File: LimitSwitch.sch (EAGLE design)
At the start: 4 parts

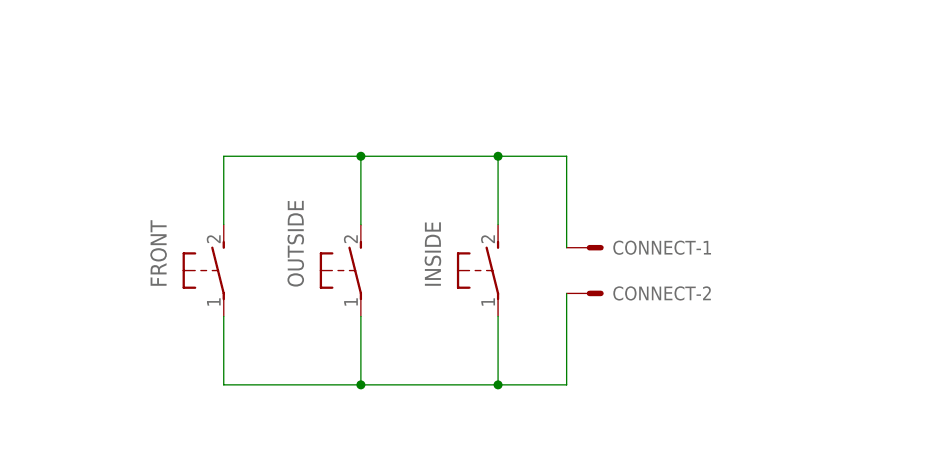
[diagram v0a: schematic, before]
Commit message: much smaller switch
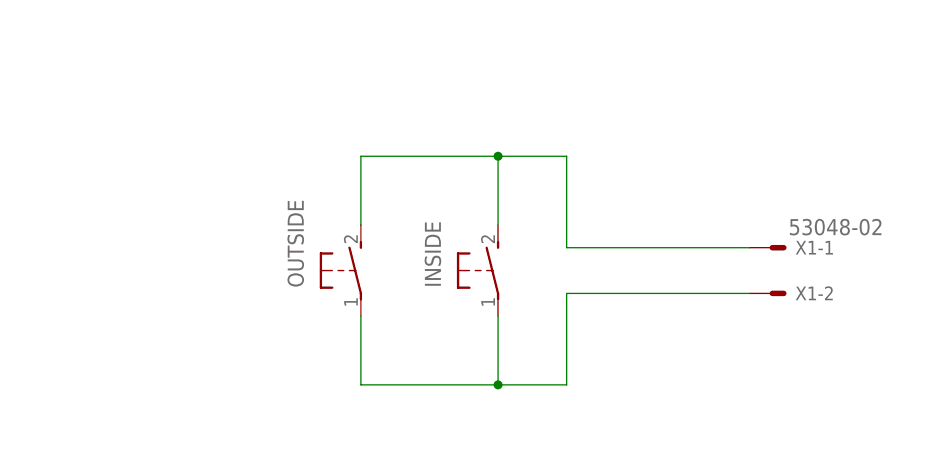
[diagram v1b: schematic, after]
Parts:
- removed CONNECT: (no value), con-molex-2:555X-2H
- removed FRONT: (no value), switch-omron:31-XX
- added X1: 53048-02, con-molex:53048-02
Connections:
- net +: now also X1-1.S; no longer CONNECT-1.S, FRONT.S
- net GND: now also X1-2.S; no longer CONNECT-2.S, FRONT.P
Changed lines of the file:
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@@
 <setting verticaltext="up"/>
 </settings>
-<grid distance="0.1" unitdist="inch" unit="inch" style="lines" multiple="1" display="yes" altdistance="0.01" altunitdist="inch" altunit="inch"/>
+<grid distance="0.1" unitdist="inch" unit="inch" style="lines" multiple="1" display="no" altdistance="0.01" altunitdist="inch" altunit="inch"/>
 <layers>
 <layer number="1" name="Top" color="4" fill="1" visible="no" active="no"/>
@@
 <parts>
 <part name="INSIDE" library="switch-omron" deviceset="31-XX" device=""/>
-<part name="CONNECT" library="con-molex-2" deviceset="555X-2" device="H"/>
 <part name="OUTSIDE" library="switch-omron" deviceset="31-XX" device=""/>
-<part name="FRONT" library="switch-omron" deviceset="31-XX" device=""/>
+<part name="X1" library="con-molex" deviceset="53?-02" device="048"/>
 </parts>
 <sheets>
@@
 </plain>
 <instances>
-<instance part="INSIDE" gate="1" x="66.04" y="53.34"/>
-<instance part="CONNECT" gate="-1" x="76.2" y="55.88"/>
-<instance part="CONNECT" gate="-2" x="76.2" y="50.8"/>
-<instance part="OUTSIDE" gate="1" x="50.8" y="53.34"/>
-<instance part="FRONT" gate="1" x="35.56" y="53.34"/>
+<instance part="INSIDE" gate="1" x="66.04" y="53.34" smashed="yes">
+<attribute name="NAME" x="59.69" y="51.435" size="1.778" layer="95" rot="R90"/>
+<attribute name="VALUE" x="62.23" y="56.515" size="1.778" layer="96" rot="R90"/>
+</instance>
+<instance part="OUTSIDE" gate="1" x="50.8" y="53.34" smashed="yes">
+<attribute name="NAME" x="44.45" y="51.435" size="1.778" layer="95" rot="R90"/>
+<attribute name="VALUE" x="46.99" y="56.515" size="1.778" layer="96" rot="R90"/>
+</instance>
+<instance part="X1" gate="-1" x="96.52" y="55.88" smashed="yes">
+<attribute name="NAME" x="99.06" y="55.118" size="1.524" layer="95"/>
+<attribute name="VALUE" x="98.298" y="57.277" size="1.778" layer="96"/>
+</instance>
+<instance part="X1" gate="-2" x="96.52" y="50.8"/>
 </instances>
 <busses>
@@
 <net name="+" class="0">
 <segment>
-<pinref part="CONNECT" gate="-1" pin="S"/>
 <wire x1="73.66" y1="55.88" x2="73.66" y2="66.04" width="0.1524" layer="91"/>
 <wire x1="73.66" y1="66.04" x2="66.04" y2="66.04" width="0.1524" layer="91"/>
-<pinref part="FRONT" gate="1" pin="S"/>
 <wire x1="66.04" y1="66.04" x2="50.8" y2="66.04" width="0.1524" layer="91"/>
-<wire x1="50.8" y1="66.04" x2="35.56" y2="66.04" width="0.1524" layer="91"/>
-<wire x1="35.56" y1="66.04" x2="35.56" y2="58.42" width="0.1524" layer="91"/>
 <pinref part="OUTSIDE" gate="1" pin="S"/>
 <wire x1="50.8" y1="58.42" x2="50.8" y2="66.04" width="0.1524" layer="91"/>
-<junction x="50.8" y="66.04"/>
 <pinref part="INSIDE" gate="1" pin="S"/>
 <wire x1="66.04" y1="58.42" x2="66.04" y2="66.04" width="0.1524" layer="91"/>
 <junction x="66.04" y="66.04"/>
+<wire x1="93.98" y1="55.88" x2="73.66" y2="55.88" width="0.1524" layer="91"/>
+<pinref part="X1" gate="-1" pin="S"/>
 </segment>
 </net>
 <net name="GND" class="0">
 <segment>
-<pinref part="CONNECT" gate="-2" pin="S"/>
 <wire x1="73.66" y1="50.8" x2="73.66" y2="40.64" width="0.1524" layer="91"/>
 <wire x1="73.66" y1="40.64" x2="66.04" y2="40.64" width="0.1524" layer="91"/>
-<pinref part="FRONT" gate="1" pin="P"/>
 <wire x1="66.04" y1="40.64" x2="50.8" y2="40.64" width="0.1524" layer="91"/>
-<wire x1="50.8" y1="40.64" x2="35.56" y2="40.64" width="0.1524" layer="91"/>
-<wire x1="35.56" y1="40.64" x2="35.56" y2="48.26" width="0.1524" layer="91"/>
 <pinref part="OUTSIDE" gate="1" pin="P"/>
 <wire x1="50.8" y1="48.26" x2="50.8" y2="40.64" width="0.1524" layer="91"/>
-<junction x="50.8" y="40.64"/>
 <pinref part="INSIDE" gate="1" pin="P"/>
 <wire x1="66.04" y1="48.26" x2="66.04" y2="40.64" width="0.1524" layer="91"/>
 <junction x="66.04" y="40.64"/>
+<wire x1="93.98" y1="50.8" x2="73.66" y2="50.8" width="0.1524" layer="91"/>
+<pinref part="X1" gate="-2" pin="S"/>
 </segment>
 </net>

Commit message: sent off an order
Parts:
- removed INSIDE, OUTSIDE: (no value), switch-omron:31-XX
- removed X1: 53048-02, con-molex:53048-02
- added C1: GRM1555C1H471FA01D, resistor:C-USC0402
- added LED1: LG Q396-PS-35, led:LEDCHIPLED_0603
- added R1: ERJ-2RKF1004X, resistor:R-US_R0402
- added S2: SKHMPSE010, switch:SKHMPSE010
- added X2: 87438-02, con-molex:87438-02
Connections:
- new net N$1: LED1.C, R1.2
- net +: now also C1.1, LED1.A, S2.1.1, X2-1.S; no longer INSIDE.S, OUTSIDE.S, X1-1.S
- net GND: now also C1.2, R1.1, S2.2.1, S2.SH, X2-2.S; no longer INSIDE.P, OUTSIDE.P, X1-2.S
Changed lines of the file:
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@@
 <layer number="97" name="Info" color="7" fill="1" visible="yes" active="yes"/>
 <layer number="98" name="Guide" color="6" fill="1" visible="yes" active="yes"/>
+<layer number="99" name="SpiceOrder" color="5" fill="1" visible="yes" active="yes"/>
 </layers>
 <schematic xreflabel="%F%N/%S.%C%R" xrefpart="/%S.%C%R">
@@
 </classes>
 <parts>
-<part name="INSIDE" library="switch-omron" deviceset="31-XX" device=""/>
-<part name="OUTSIDE" library="switch-omron" deviceset="31-XX" device=""/>
-<part name="X1" library="con-molex" deviceset="53?-02" device="048"/>
+<part name="X2" library="con-molex" deviceset="87438-02" device=""/>
+<part name="S2" library="switch" deviceset="SKHMP*E010" device="" technology="S"/>
+<part name="R1" library="resistor" deviceset="R-US_" device="R0402" value="ERJ-2RKF1004X"/>
+<part name="C1" library="resistor" deviceset="C-US" device="C0402" value="GRM1555C1H471FA01D"/>
+<part name="LED1" library="led" deviceset="LED" device="CHIPLED_0603" value="LG Q396-PS-35"/>
 </parts>
 <sheets>
@@
 </plain>
 <instances>
-<instance part="INSIDE" gate="1" x="66.04" y="53.34" smashed="yes">
-<attribute name="NAME" x="59.69" y="51.435" size="1.778" layer="95" rot="R90"/>
-<attribute name="VALUE" x="62.23" y="56.515" size="1.778" layer="96" rot="R90"/>
-</instance>
-<instance part="OUTSIDE" gate="1" x="50.8" y="53.34" smashed="yes">
-<attribute name="NAME" x="44.45" y="51.435" size="1.778" layer="95" rot="R90"/>
-<attribute name="VALUE" x="46.99" y="56.515" size="1.778" layer="96" rot="R90"/>
-</instance>
-<instance part="X1" gate="-1" x="96.52" y="55.88" smashed="yes">
-<attribute name="NAME" x="99.06" y="55.118" size="1.524" layer="95"/>
-<attribute name="VALUE" x="98.298" y="57.277" size="1.778" layer="96"/>
-</instance>
-<instance part="X1" gate="-2" x="96.52" y="50.8"/>
+<instance part="X2" gate="-1" x="96.52" y="55.88"/>
+<instance part="X2" gate="-2" x="96.52" y="48.26"/>
+<instance part="S2" gate="G$1" x="25.4" y="53.34" rot="R90"/>
+<instance part="R1" gate="G$1" x="45.72" y="45.72" rot="R90"/>
+<instance part="C1" gate="G$1" x="76.2" y="53.34"/>
+<instance part="LED1" gate="G$1" x="45.72" y="60.96"/>
 </instances>
 <busses>
@@
 <net name="+" class="0">
 <segment>
-<wire x1="73.66" y1="55.88" x2="73.66" y2="66.04" width="0.1524" layer="91"/>
-<wire x1="73.66" y1="66.04" x2="66.04" y2="66.04" width="0.1524" layer="91"/>
-<wire x1="66.04" y1="66.04" x2="50.8" y2="66.04" width="0.1524" layer="91"/>
-<pinref part="OUTSIDE" gate="1" pin="S"/>
-<wire x1="50.8" y1="58.42" x2="50.8" y2="66.04" width="0.1524" layer="91"/>
-<pinref part="INSIDE" gate="1" pin="S"/>
-<wire x1="66.04" y1="58.42" x2="66.04" y2="66.04" width="0.1524" layer="91"/>
-<junction x="66.04" y="66.04"/>
-<wire x1="93.98" y1="55.88" x2="73.66" y2="55.88" width="0.1524" layer="91"/>
-<pinref part="X1" gate="-1" pin="S"/>
+<wire x1="93.98" y1="55.88" x2="76.2" y2="55.88" width="0.1524" layer="91"/>
+<label x="91.44" y="58.42" size="1.778" layer="95"/>
+<pinref part="X2" gate="-1" pin="S"/>
+<pinref part="C1" gate="G$1" pin="1"/>
+<wire x1="73.66" y1="78.74" x2="73.66" y2="55.88" width="0.1524" layer="91"/>
+<wire x1="73.66" y1="78.74" x2="45.72" y2="78.74" width="0.1524" layer="91"/>
+<label x="60.96" y="78.74" size="1.778" layer="95"/>
+<wire x1="45.72" y1="78.74" x2="12.7" y2="78.74" width="0.1524" layer="91"/>
+<wire x1="12.7" y1="78.74" x2="12.7" y2="45.72" width="0.1524" layer="91"/>
+<wire x1="12.7" y1="45.72" x2="25.4" y2="45.72" width="0.1524" layer="91"/>
+<pinref part="S2" gate="G$1" pin="1.1"/>
+<wire x1="25.4" y1="45.72" x2="25.4" y2="48.26" width="0.1524" layer="91"/>
+<wire x1="76.2" y1="55.88" x2="73.66" y2="55.88" width="0.1524" layer="91"/>
+<junction x="76.2" y="55.88"/>
+<pinref part="LED1" gate="G$1" pin="A"/>
+<wire x1="45.72" y1="78.74" x2="45.72" y2="63.5" width="0.1524" layer="91"/>
+<junction x="45.72" y="78.74"/>
 </segment>
 </net>
 <net name="GND" class="0">
 <segment>
-<wire x1="73.66" y1="50.8" x2="73.66" y2="40.64" width="0.1524" layer="91"/>
-<wire x1="73.66" y1="40.64" x2="66.04" y2="40.64" width="0.1524" layer="91"/>
-<wire x1="66.04" y1="40.64" x2="50.8" y2="40.64" width="0.1524" layer="91"/>
-<pinref part="OUTSIDE" gate="1" pin="P"/>
-<wire x1="50.8" y1="48.26" x2="50.8" y2="40.64" width="0.1524" layer="91"/>
-<pinref part="INSIDE" gate="1" pin="P"/>
-<wire x1="66.04" y1="48.26" x2="66.04" y2="40.64" width="0.1524" layer="91"/>
-<junction x="66.04" y="40.64"/>
-<wire x1="93.98" y1="50.8" x2="73.66" y2="50.8" width="0.1524" layer="91"/>
-<pinref part="X1" gate="-2" pin="S"/>
+<label x="88.9" y="45.72" size="1.778" layer="95"/>
+<wire x1="73.66" y1="48.26" x2="73.66" y2="35.56" width="0.1524" layer="91"/>
+<pinref part="S2" gate="G$1" pin="SH"/>
+<wire x1="30.48" y1="48.26" x2="30.48" y2="35.56" width="0.1524" layer="91"/>
+<wire x1="30.48" y1="35.56" x2="45.72" y2="35.56" width="0.1524" layer="91"/>
+<junction x="30.48" y="35.56"/>
+<pinref part="X2" gate="-2" pin="S"/>
+<wire x1="45.72" y1="35.56" x2="73.66" y2="35.56" width="0.1524" layer="91"/>
+<wire x1="73.66" y1="48.26" x2="76.2" y2="48.26" width="0.1524" layer="91"/>
+<pinref part="S2" gate="G$1" pin="2.1"/>
+<wire x1="76.2" y1="48.26" x2="93.98" y2="48.26" width="0.1524" layer="91"/>
+<wire x1="25.4" y1="60.96" x2="17.78" y2="60.96" width="0.1524" layer="91"/>
+<wire x1="17.78" y1="60.96" x2="17.78" y2="35.56" width="0.1524" layer="91"/>
+<wire x1="17.78" y1="35.56" x2="30.48" y2="35.56" width="0.1524" layer="91"/>
+<pinref part="C1" gate="G$1" pin="2"/>
+<junction x="76.2" y="48.26"/>
+<pinref part="R1" gate="G$1" pin="1"/>
+<wire x1="45.72" y1="40.64" x2="45.72" y2="35.56" width="0.1524" layer="91"/>
+<junction x="45.72" y="35.56"/>
 </segment>
 </net>
+<net name="N$1" class="0">
+<segment>
+<pinref part="LED1" gate="G$1" pin="C"/>
+<pinref part="R1" gate="G$1" pin="2"/>
+<wire x1="45.72" y1="55.88" x2="45.72" y2="50.8" width="0.1524" layer="91"/>
+</segment>
+</net>
